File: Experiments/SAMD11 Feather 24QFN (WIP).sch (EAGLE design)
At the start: 30 parts, among them IC1 ATSAMD11D14A-SSNT, J1 10118193-0001LF, Q1 DMG341, SW1 SPST_TACT-KMR2, U1 AP2112-3.3, U2 MCP73831T-2ACI/OT, X1 JSTPH, X2 2x5 0.05" SWD

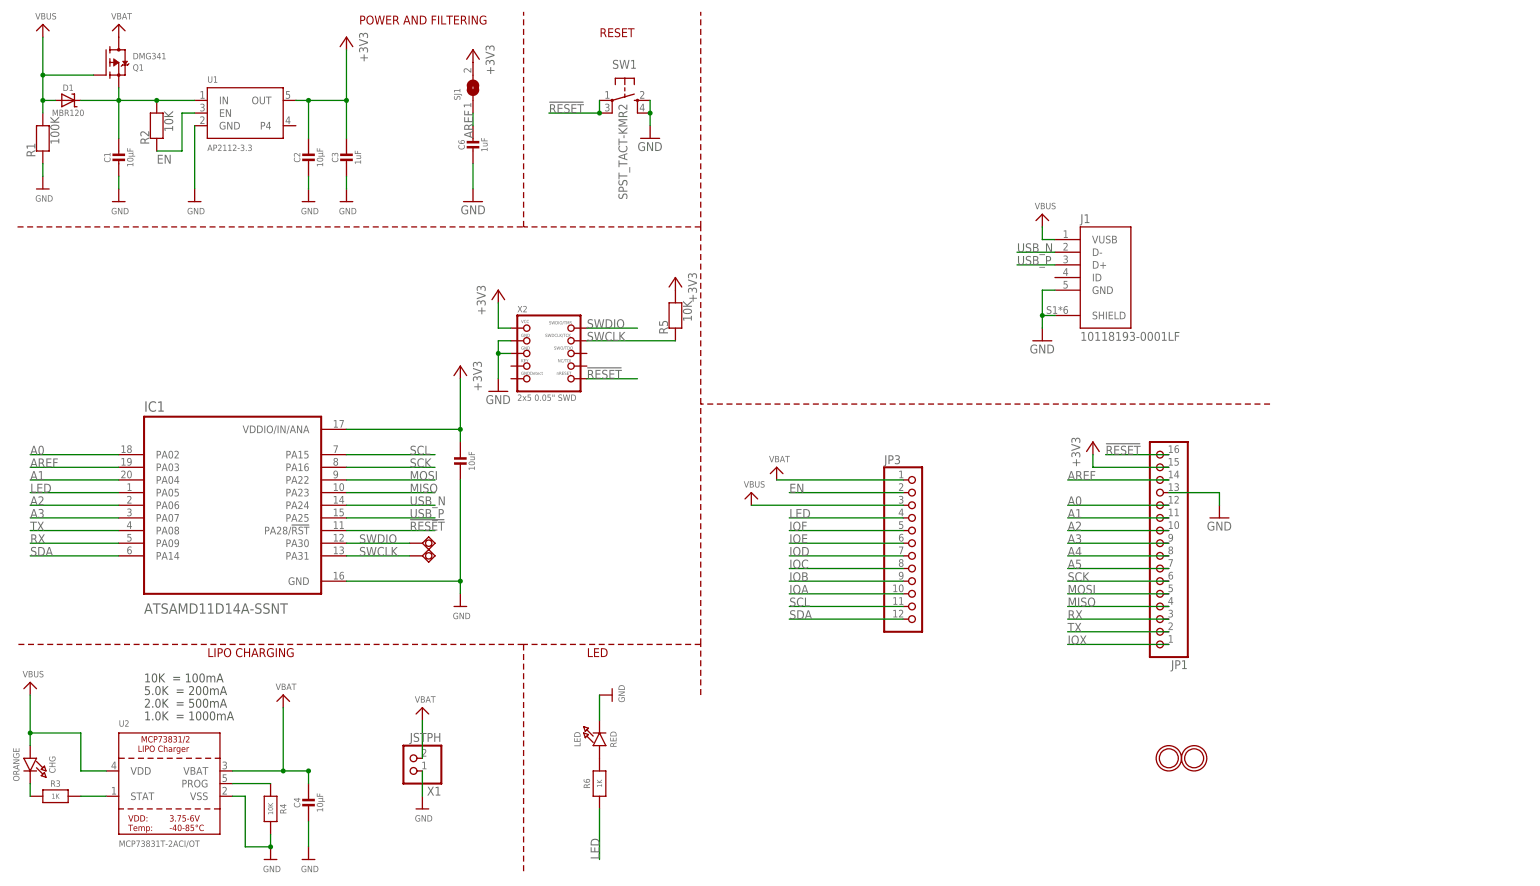
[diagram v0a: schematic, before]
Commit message: first rev of the hand-solderable one, WIP the QFN package
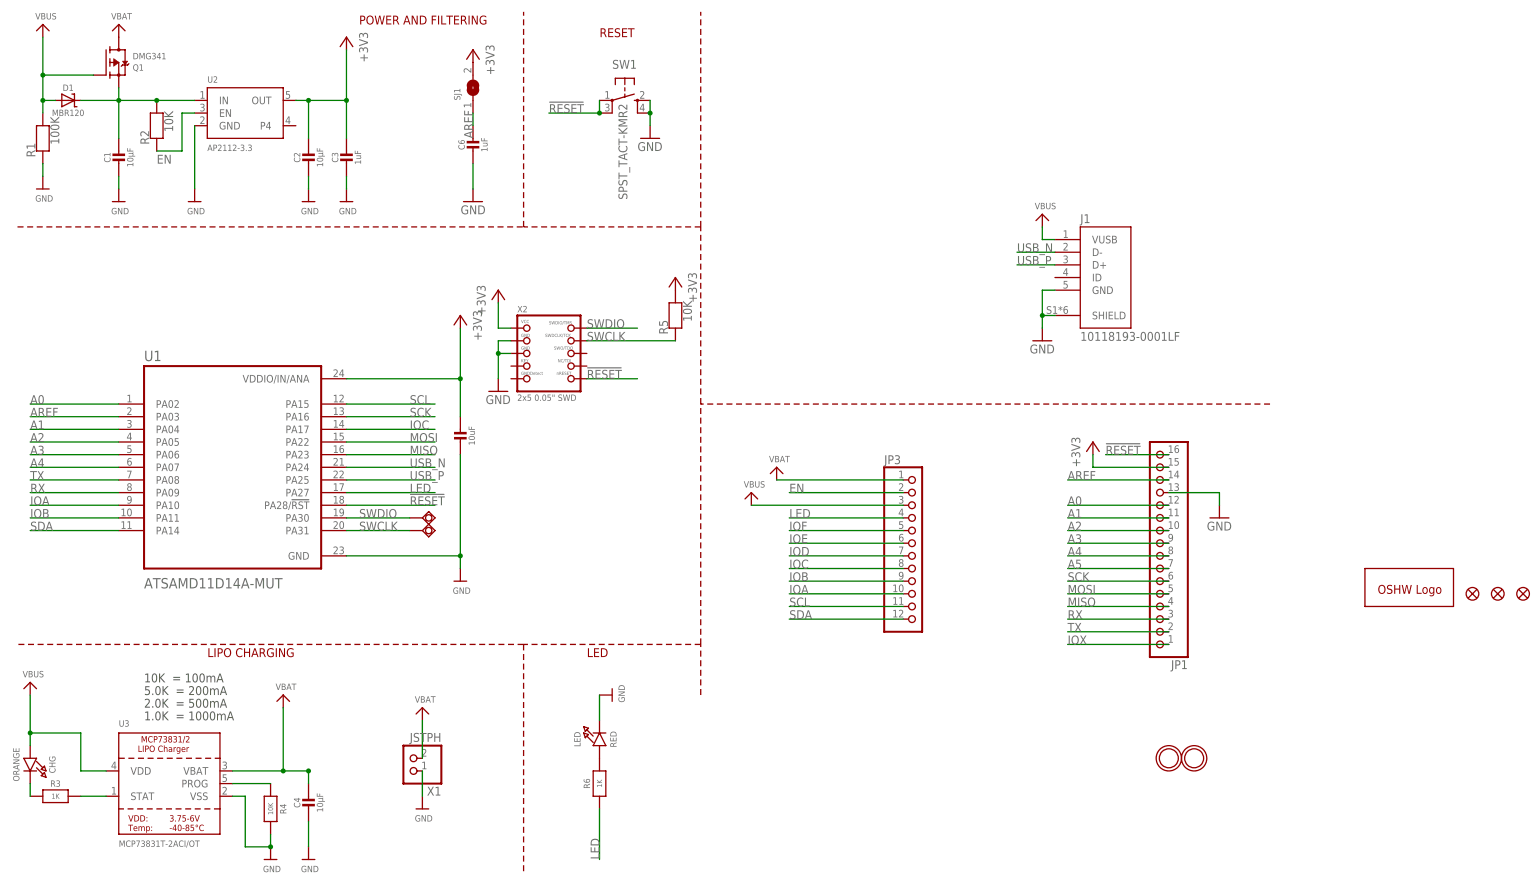
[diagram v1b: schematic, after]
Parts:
- removed IC1: ATSAMD11D14A-SSNT, ATSAMD11D14A-SSNT:ATSAMD11D14A-SSNT
- added FID1, FID3, FID4: FIDUCIAL_1MM, microbuilder:FIDUCIAL_1MM
- added GOLD_ORB_SM1: OSHWLOGOLOGO5MM, oshw:OSHWLOGOLOGO5MM
- added U3: MCP73831T-2ACI/OT, microbuilder:MCP73831/2
- U1: value AP2112-3.3 -> ATSAMD11D14A-MUT; device microbuilder:VREG_SOT23-5 -> ATSAMD11D14A-MUT:ATSAMD11D14A-MUT
- U2: value MCP73831T-2ACI/OT -> AP2112-3.3; device microbuilder:MCP73831/2 -> microbuilder:VREG_SOT23-5
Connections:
- net !RESET: now also U1.PA28/!RST; no longer IC1.PA28/!RST
- net +3V3: now also U1.VDDIO/IN/ANA, U2.OUT; no longer IC1.VDDIO/IN/ANA, U1.OUT
- net A0: now also U1.PA02; no longer IC1.PA02
- net A1: now also U1.PA04; no longer IC1.PA04
- net A2: now also U1.PA05; no longer IC1.PA06
- net A3: now also U1.PA06; no longer IC1.PA07
- net A4: now also U1.PA07
- net AREF: now also U1.PA03; no longer IC1.PA03
- net EN: now also U2.EN; no longer U1.EN
- net GND: now also U2.GND, U3.VSS; no longer IC1.GND, U2.VSS
- net IOA: now also U1.PA10
- net IOB: now also U1.PA11
- net IOC: now also U1.PA17
- net LED: now also U1.PA27; no longer IC1.PA05
- net MISO: now also U1.PA23; no longer IC1.PA23
- net MOSI: now also U1.PA22; no longer IC1.PA22
- net PROG: now also U3.PROG; no longer U2.PROG
- net RX: now also U1.PA09; no longer IC1.PA09
- net SCK: now also U1.PA16; no longer IC1.PA16
- net SCL: now also U1.PA15; no longer IC1.PA15
- net SDA: now also U1.PA14; no longer IC1.PA14
- net STAT: now also U3.STAT; no longer U2.STAT
- net SWCLK: now also U1.PA31; no longer IC1.PA31
- net SWDIO: now also U1.PA30; no longer IC1.PA30
- net TX: now also U1.PA08; no longer IC1.PA08
- net USB_N: now also U1.PA24; no longer IC1.PA24
- net USB_P: now also U1.PA25; no longer IC1.PA25
- net VBAT: now also U3.VBAT; no longer U2.VBAT
- net VBUS: now also U3.VDD; no longer U2.VDD
- net VHI: now also U2.IN; no longer U1.IN

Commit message: tweak some silkscreen text
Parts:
- removed U3: MCP73831T-2ACI/OT, microbuilder:MCP73831/2
- added IC1: ATSAMD11D14A-MUT, ATSAMD11D14A-MUT:ATSAMD11D14A-MUT
- U1: value ATSAMD11D14A-MUT -> AP2112-3.3; device ATSAMD11D14A-MUT:ATSAMD11D14A-MUT -> microbuilder:VREG_SOT23-5
- U2: value AP2112-3.3 -> MCP73831T-2ACI/OT; device microbuilder:VREG_SOT23-5 -> microbuilder:MCP73831/2
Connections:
- net !RESET: now also IC1.PA28/!RST; no longer U1.PA28/!RST
- net +3V3: now also IC1.VDDIO/IN/ANA, U1.OUT; no longer U1.VDDIO/IN/ANA, U2.OUT
- net A0: now also IC1.PA02; no longer U1.PA02
- net A1: now also IC1.PA04; no longer U1.PA04
- net A2: now also IC1.PA05; no longer U1.PA05
- net A3: now also IC1.PA06; no longer U1.PA06
- net A4: now also IC1.PA07; no longer U1.PA07
- net AREF: now also IC1.PA03; no longer U1.PA03
- net EN: now also U1.EN; no longer U2.EN
- net GND: now also IC1.GND, U2.VSS; no longer U2.GND, U3.VSS
- net IOA: now also IC1.PA10; no longer U1.PA10
- net IOB: now also IC1.PA11; no longer U1.PA11
- net IOC: now also IC1.PA17; no longer U1.PA17
- net LED: now also IC1.PA27; no longer U1.PA27
- net MISO: now also IC1.PA23; no longer U1.PA23
- net MOSI: now also IC1.PA22; no longer U1.PA22
- net PROG: now also U2.PROG; no longer U3.PROG
- net RX: now also IC1.PA09; no longer U1.PA09
- net SCK: now also IC1.PA16; no longer U1.PA16
- net SCL: now also IC1.PA15; no longer U1.PA15
- net SDA: now also IC1.PA14; no longer U1.PA14
- net STAT: now also U2.STAT; no longer U3.STAT
- net SWCLK: now also IC1.PA31; no longer U1.PA31
- net SWDIO: now also IC1.PA30; no longer U1.PA30
- net TX: now also IC1.PA08; no longer U1.PA08
- net USB_N: now also IC1.PA24; no longer U1.PA24
- net USB_P: now also IC1.PA25; no longer U1.PA25
- net VBAT: now also U2.VBAT; no longer U3.VBAT
- net VBUS: now also U2.VDD; no longer U3.VDD
- net VHI: now also U1.IN; no longer U2.IN

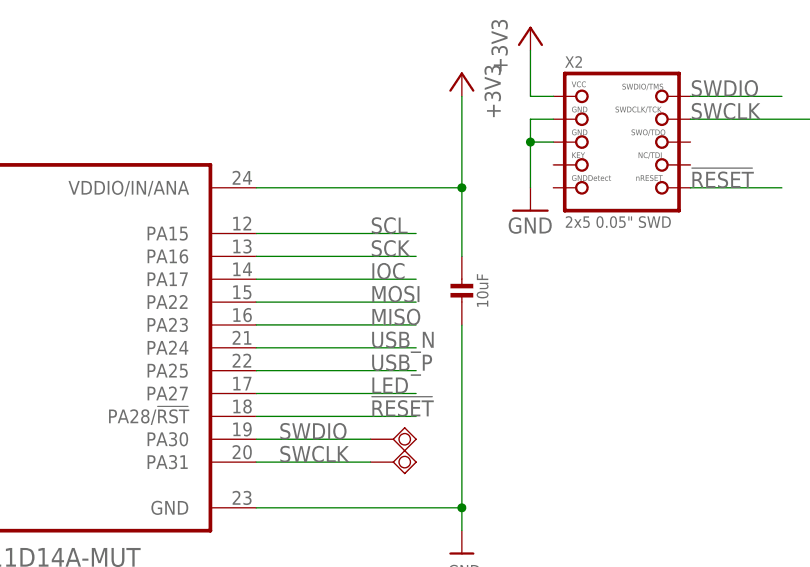
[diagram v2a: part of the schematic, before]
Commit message: swap miso and sck to match intended muxing
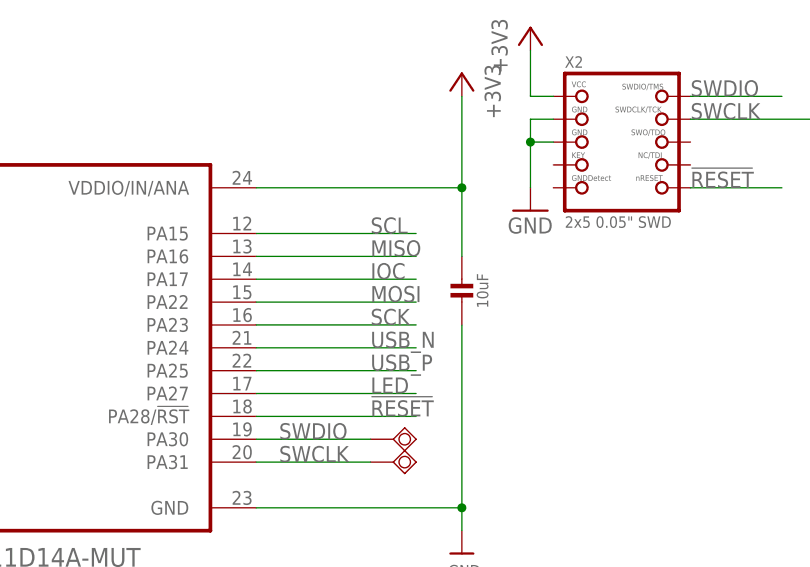
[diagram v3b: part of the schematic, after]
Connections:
- net MISO: now also IC1.PA16; no longer IC1.PA23
- net SCK: now also IC1.PA23; no longer IC1.PA16
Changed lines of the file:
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@@
 </segment>
 <segment>
-<wire x1="71.12" y1="86.36" x2="88.9" y2="86.36" width="0.1524" layer="91"/>
-<label x="83.82" y="86.36" size="1.778" layer="95"/>
-<pinref part="IC1" gate="G$1" pin="PA23"/>
+<wire x1="71.12" y1="93.98" x2="88.9" y2="93.98" width="0.1524" layer="91"/>
+<pinref part="IC1" gate="G$1" pin="PA16"/>
+<label x="83.82" y="93.98" size="1.778" layer="95"/>
 </segment>
 </net>
@@
 </segment>
 <segment>
-<wire x1="71.12" y1="93.98" x2="88.9" y2="93.98" width="0.1524" layer="91"/>
-<label x="83.82" y="93.98" size="1.778" layer="95"/>
-<pinref part="IC1" gate="G$1" pin="PA16"/>
+<wire x1="71.12" y1="86.36" x2="88.9" y2="86.36" width="0.1524" layer="91"/>
+<pinref part="IC1" gate="G$1" pin="PA23"/>
+<label x="83.82" y="86.36" size="1.778" layer="95"/>
 </segment>
 </net>
